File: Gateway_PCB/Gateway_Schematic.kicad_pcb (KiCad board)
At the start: 2 copper layers, 44.4 x 63.5 mm, 9 parts, among them J1 Conn_01x40_Female, J2 Conn_01x08_Female, J3 Conn_01x08_Female, J4 Conn_01x01_Female

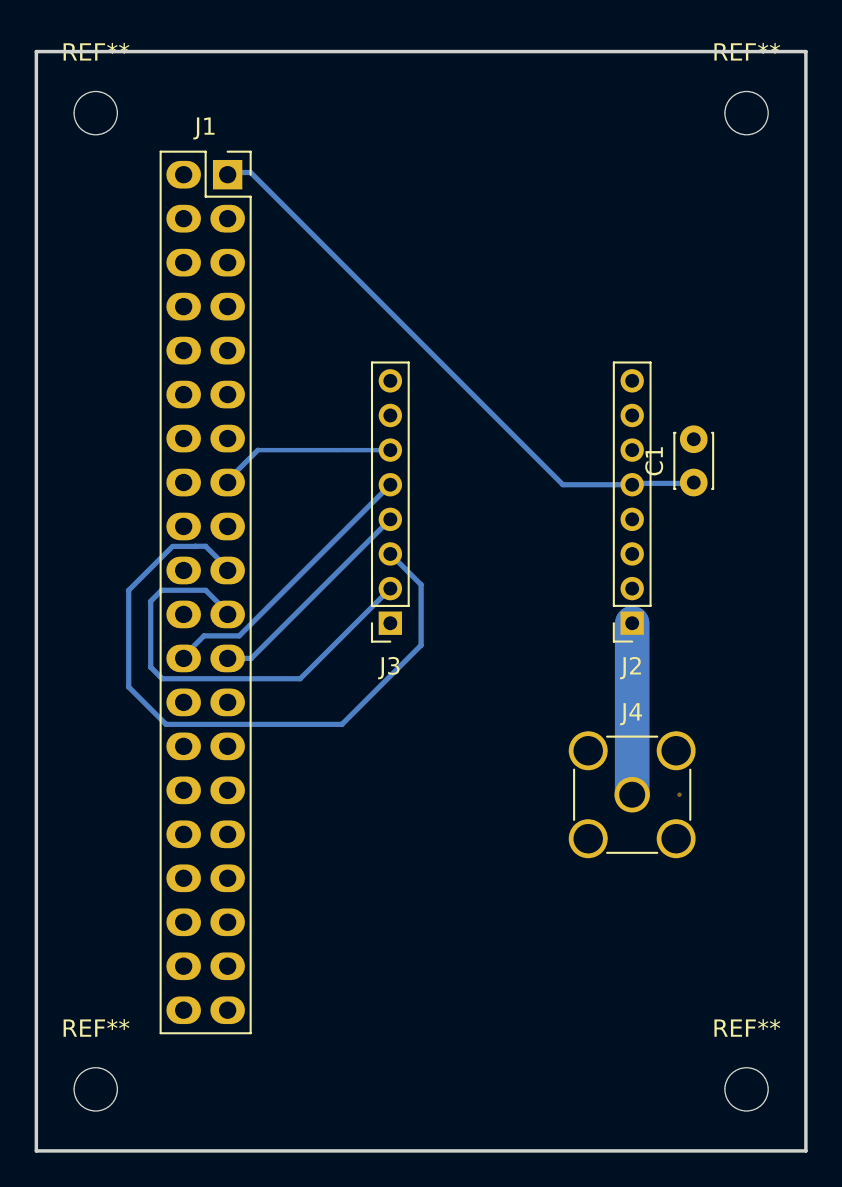
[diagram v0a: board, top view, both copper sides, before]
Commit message: Changed RFM95W footprint and added SMA Connector Model
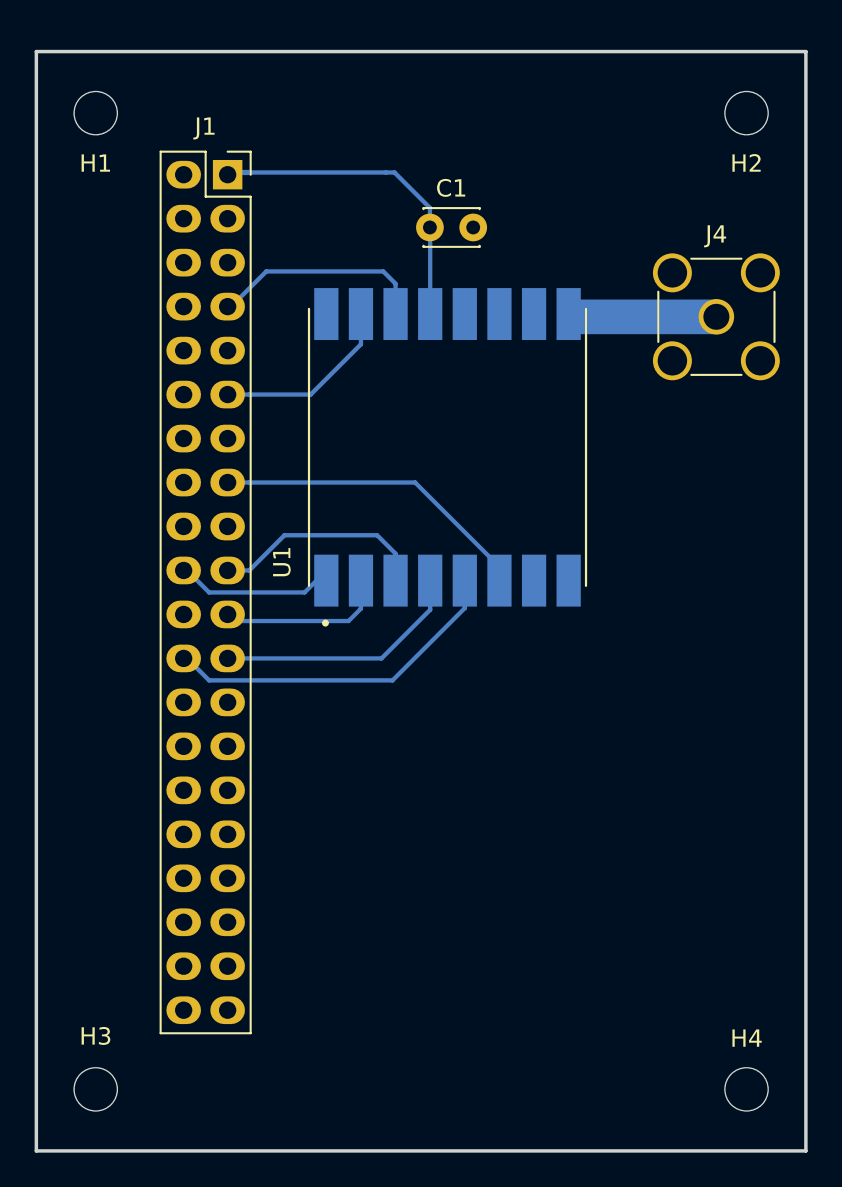
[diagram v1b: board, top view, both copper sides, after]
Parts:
- removed J2, J3: Conn_01x08_Female, Connector_PinSocket_2.00mm:PinSocket_1x08_P2.00mm_Vertical
- added U1: RFM95W-868S2, RFM95:XCVR_RFM95W-915S2, F.Cu at (119.0, 86.4)
- moved J4 28.0 mm to (134.5, 78.8)
- moved C1 21.2 mm to (118.0, 73.7), turned to 0 degrees
- renumbered REF** to H1, REF** to H2, REF** to H3, REF** to H4
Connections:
- J1 pad 20: Net-(J1-Pad20) -> GND
- J1 pad 39: Net-(J1-Pad39) -> GND
- J1 pad 9: GND -> Net-(J1-Pad9)
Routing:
- net MOSI: track 38.6 -> 12.5 mm
- net (no net): track 17.3 -> 0.00 mm
- net +3V3: track 35.3 -> 18.7 mm
- net DIO0: track 0.00 -> 12.6 mm
- net DIO1: track 0.00 -> 10.7 mm
- net GND: track 0.00 -> 9.05 mm
- net RST: track 10.1 -> 18.5 mm
- net MISO: track 18.0 -> 9.77 mm
- net ANT: track 0.01 -> 7.83 mm
- net NSS: track 16.0 -> 20.1 mm
- net SCK: track 12.7 -> 14.5 mm
